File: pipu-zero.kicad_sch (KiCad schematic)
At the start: 4 parts, among them J1 USB_C_Receptacle_USB2.0_14P

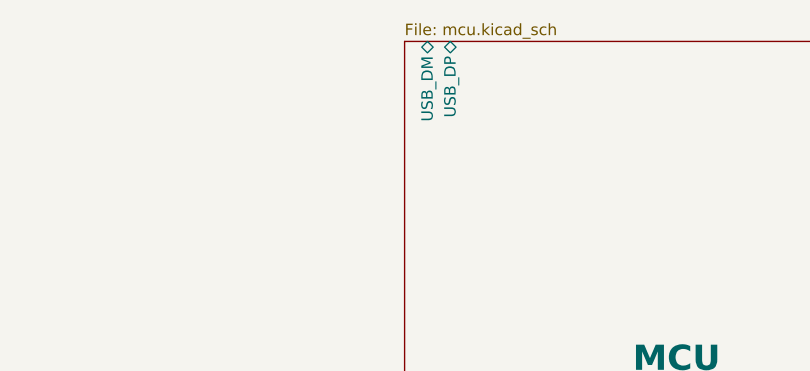
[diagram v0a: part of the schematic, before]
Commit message: add missing connections inside MCU
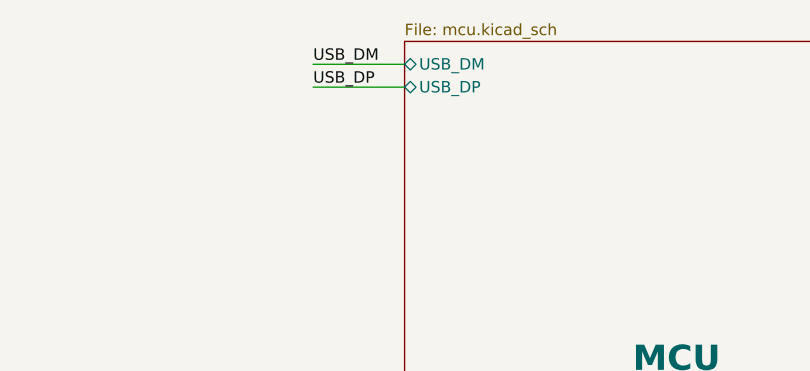
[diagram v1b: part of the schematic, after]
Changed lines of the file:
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@@
+	(wire
+		(pts
+			(xy 138.43 44.45) (xy 148.59 44.45)
+		)
+		(stroke
+			(width 0)
+			(type default)
+		)
+	)
 	(wire
 		(pts
@@
 		(pts
 			(xy 208.28 100.33) (xy 219.71 100.33)
+		)
+		(stroke
+			(width 0)
+			(type default)
+		)
+	)
+	(wire
+		(pts
+			(xy 138.43 46.99) (xy 148.59 46.99)
 		)
 		(stroke
@@
 		)
 	)
+	(label "USB_DM"
+		(at 138.43 44.45 0)
+		(effects
+			(font
+				(size 1.27 1.27)
+			)
+			(justify left bottom)
+		)
+	)
 	(label "USB_VBUS"
 		(at 72.39 85.09 180)
@@
 			)
 			(justify right bottom)
+		)
+	)
+	(label "USB_DP"
+		(at 138.43 46.99 0)
+		(effects
+			(font
+				(size 1.27 1.27)
+			)
+			(justify left bottom)
 		)
 	)
@@
 		)
 		(pin "USB_DM" bidirectional
-			(at 151.13 41.91 90)
-			(effects
-				(font
-					(size 1.27 1.27)
-				)
-				(justify right)
+			(at 148.59 44.45 180)
+			(effects
+				(font
+					(size 1.27 1.27)
+				)
+				(justify left)
 			)
 		)
 		(pin "USB_DP" bidirectional
-			(at 153.67 41.91 90)
-			(effects
-				(font
-					(size 1.27 1.27)
-				)
-				(justify right)
-			)
-		)
+			(at 148.59 46.99 180)
+			(effects
+				(font
+					(size 1.27 1.27)
+				)
+				(justify left)
+			)
+		)

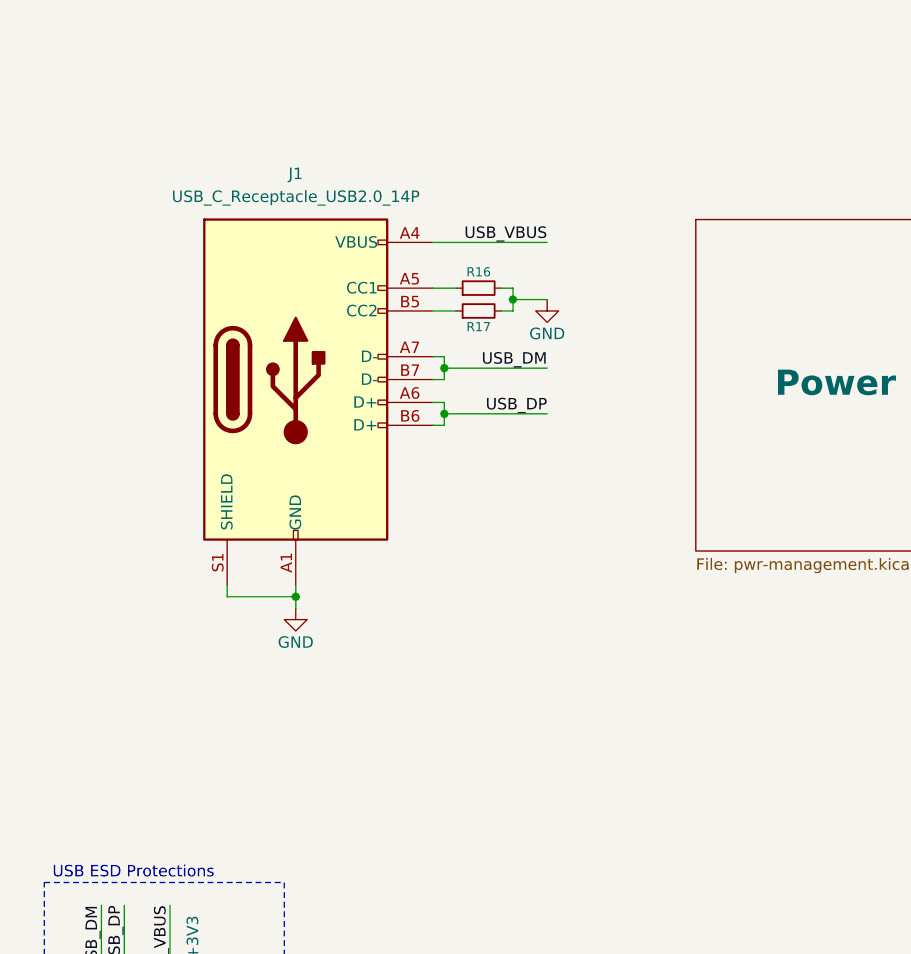
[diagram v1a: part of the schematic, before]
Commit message: add boost converter and ldo regulator
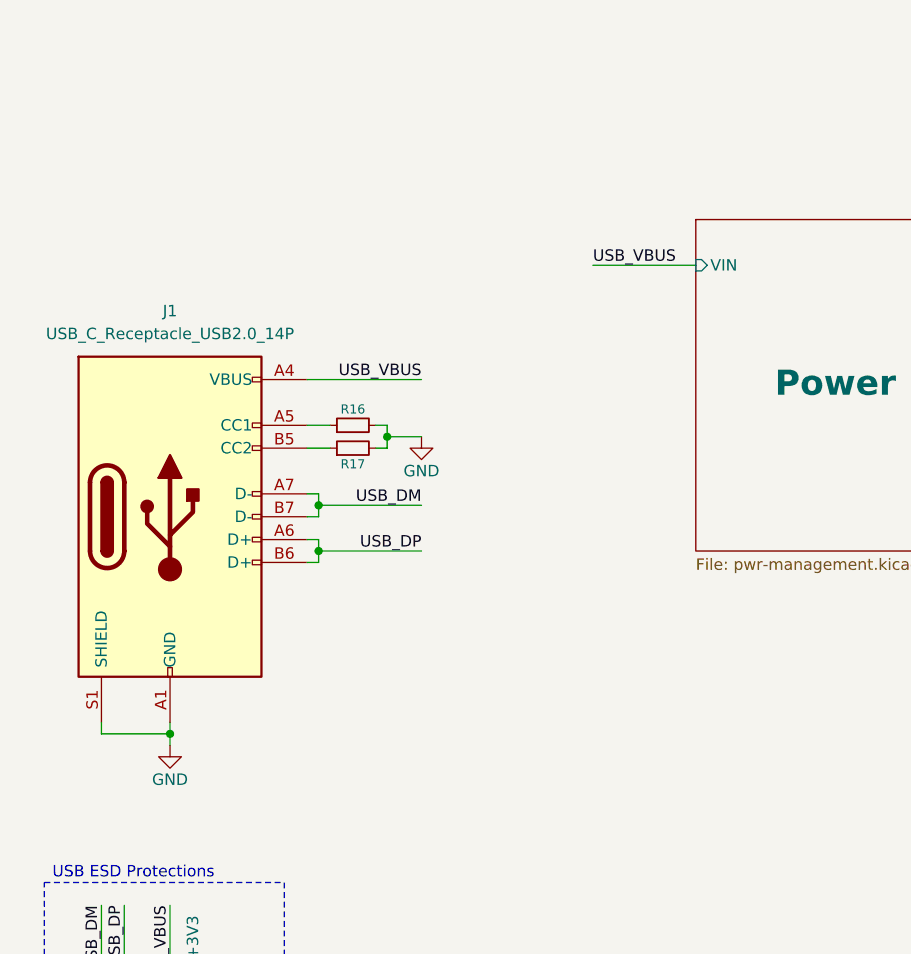
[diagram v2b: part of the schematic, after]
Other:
- sheet Power Manager ports: added VIN; removed none
- moved on the sheet: J1, R16, R17

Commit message: set initial component footprints
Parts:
- R1: renamed from R16; footprint (none) -> Resistor_SMD:R_0603_1608Metric
- R2: renamed from R17; footprint (none) -> Resistor_SMD:R_0603_1608Metric
- renumbered D5 to D1
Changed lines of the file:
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@@
 		(on_board yes)
 		(dnp no)
-		(property "Reference" "R16"
+		(property "Reference" "R1"
 			(at 50.8 103.632 90)
 			(effects
@@
 			)
 		)
-		(property "Footprint" ""
+		(property "Footprint" "Resistor_SMD:R_0603_1608Metric"
 			(at 50.8 105.41 0)
 			(effects
@@
 			(project ""
 				(path "/3130e1f2-bde1-4b12-bd54-0e1e50bd36da"
-					(reference "R16")
+					(reference "R1")
 					(unit 1)
 				)
@@
 		(on_board yes)
 		(dnp no)
-		(property "Reference" "R17"
+		(property "Reference" "R2"
 			(at 50.8 109.728 90)
 			(effects
@@
 			)
 		)
-		(property "Footprint" ""
+		(property "Footprint" "Resistor_SMD:R_0603_1608Metric"
 			(at 50.8 107.95 0)
 			(effects
@@
 			(project "pipu-zero"
 				(path "/3130e1f2-bde1-4b12-bd54-0e1e50bd36da"
-					(reference "R17")
+					(reference "R2")
 					(unit 1)
 				)
@@
 		(on_board yes)
 		(dnp no)
-		(property "Reference" "#PWR035"
+		(property "Reference" "#PWR02"
 			(at 30.48 147.32 0)
 			(effects
@@
 			(project ""
 				(path "/3130e1f2-bde1-4b12-bd54-0e1e50bd36da"
-					(reference "#PWR035")
+					(reference "#PWR02")
 					(unit 1)
 				)
@@
 		(on_board yes)
 		(dnp no)
-		(property "Reference" "#PWR036"
+		(property "Reference" "#PWR04"
 			(at 58.42 113.03 0)
 			(effects
@@
 			(project ""
 				(path "/3130e1f2-bde1-4b12-bd54-0e1e50bd36da"
-					(reference "#PWR036")
+					(reference "#PWR04")
 					(unit 1)
 				)
@@
 		(on_board yes)
 		(dnp no)
-		(property "Reference" "#PWR037"
+		(property "Reference" "#PWR03"
 			(at 33.02 171.45 0)
 			(effects
@@
 			(project ""
 				(path "/3130e1f2-bde1-4b12-bd54-0e1e50bd36da"
-					(reference "#PWR037")
+					(reference "#PWR03")
 					(unit 1)
 				)
@@
 		(on_board yes)
 		(dnp no)
-		(property "Reference" "D5"
+		(property "Reference" "D1"
 			(at 37.338 182.626 90)
 			(effects
@@
 			(project "pipu-zero"
 				(path "/3130e1f2-bde1-4b12-bd54-0e1e50bd36da"
-					(reference "D5")
+					(reference "D1")
 					(unit 1)
 				)
@@
 		(on_board yes)
 		(dnp no)
-		(property "Reference" "#PWR034"
+		(property "Reference" "#PWR01"
 			(at 27.94 193.04 0)
 			(effects
@@
 			(project ""
 				(path "/3130e1f2-bde1-4b12-bd54-0e1e50bd36da"
-					(reference "#PWR034")
-					(unit 1)
-				)
+					(reference "#PWR01")
+					(unit 1)
+				)

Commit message: Add footprints
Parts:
- J1: footprint (none) -> USBC:HRO_TYPE-C-31-M-12
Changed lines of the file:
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@@
 			)
 		)
-		(property "Footprint" ""
+		(property "Footprint" "USBC:HRO_TYPE-C-31-M-12"
 			(at 34.29 115.57 0)
 			(effects

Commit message: modify ios
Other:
- sheet I-O ports: added IO39, IO40, IO41, IO42; removed IO0, IO14, IO3, IO38, IO46, IO9
- sheet MCU ports: added IO39, IO40, IO41, IO42; removed IO0, IO14, IO3, IO38, IO46, IO9
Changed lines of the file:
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@@
-	(wire
-		(pts
-			(xy 208.28 64.77) (xy 219.71 64.77)
-		)
-		(stroke
-			(width 0)
-			(type default)
-		)
-	)
 	(wire
 		(pts
@@
 		(pts
 			(xy 46.99 114.3) (xy 58.42 114.3)
-		)
-		(stroke
-			(width 0)
-			(type default)
-		)
-	)
-	(wire
-		(pts
-			(xy 208.28 62.23) (xy 219.71 62.23)
 		)
 		(stroke
@@
 			)
 		)
-		(pin "IO0" bidirectional
+		(pin "IO39" bidirectional
 			(at 219.71 52.07 180)
 			(effects
@@
 			)
 		)
-		(pin "IO3" bidirectional
+		(pin "IO40" bidirectional
 			(at 219.71 54.61 180)
 			(effects
@@
 			)
 		)
-		(pin "IO9" bidirectional
+		(pin "IO41" bidirectional
 			(at 219.71 57.15 180)
 			(effects
@@
 			)
 		)
-		(pin "IO14" bidirectional
+		(pin "IO42" bidirectional
 			(at 219.71 59.69 180)
-			(effects
-				(font
-					(size 1.27 1.27)
-				)
-				(justify left)
-			)
-		)
-		(pin "IO38" bidirectional
-			(at 219.71 62.23 180)
-			(effects
-				(font
-					(size 1.27 1.27)
-				)
-				(justify left)
-			)
-		)
-		(pin "IO46" bidirectional
-			(at 219.71 64.77 180)
 			(effects
 				(font
@@
 			)
 		)
-		(pin "IO0" bidirectional
-			(at 208.28 52.07 0)
-			(effects
-				(font
-					(size 1.27 1.27)
-				)
-				(justify right)
-			)
-		)
-		(pin "IO3" bidirectional
-			(at 208.28 54.61 0)
-			(effects
-				(font
-					(size 1.27 1.27)
-				)
-				(justify right)
-			)
-		)
-		(pin "IO9" bidirectional
-			(at 208.28 57.15 0)
-			(effects
-				(font
-					(size 1.27 1.27)
-				)
-				(justify right)
-			)
-		)
-		(pin "IO14" bidirectional
-			(at 208.28 59.69 0)
-			(effects
-				(font
-					(size 1.27 1.27)
-				)
-				(justify right)
-			)
-		)
-		(pin "IO38" bidirectional
-			(at 208.28 62.23 0)
-			(effects
-				(font
-					(size 1.27 1.27)
-				)
-				(justify right)
-			)
-		)
-		(pin "IO46" bidirectional
-			(at 208.28 64.77 0)
-			(effects
-				(font
-					(size 1.27 1.27)
-				)
-				(justify right)
-			)
-		)
 		(pin "RXD0" bidirectional
 			(at 208.28 67.31 0)
@@
 			(effects
 				(font
+					(size 1.27 1.27)
+				)
+				(justify right)
+			)
+		)
+		(pin "IO40" bidirectional
+			(at 208.28 54.61 0)
+			(effects
+				(font
+					(size 1.27 1.27)
+				)
+				(justify right)
+			)
+		)
+		(pin "IO41" bidirectional
+			(at 208.28 57.15 0)
+			(effects
+				(font
+					(size 1.27 1.27)
+				)
+				(justify right)
+			)
+		)
+		(pin "IO42" bidirectional
+			(at 208.28 59.69 0)
+			(effects
+				(font
+					(size 1.27 1.27)
+				)
+				(justify right)
+			)
+		)
+		(pin "IO39" bidirectional
+			(at 208.28 52.07 0)
+			(effects
+				(font

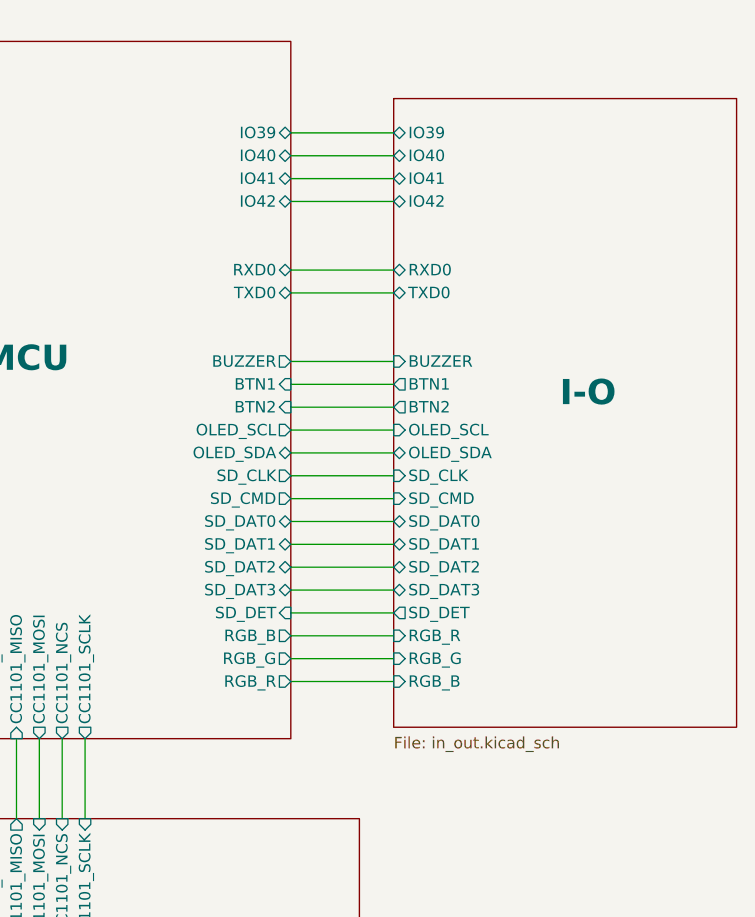
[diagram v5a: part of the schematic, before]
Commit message: Add encoder to schematic
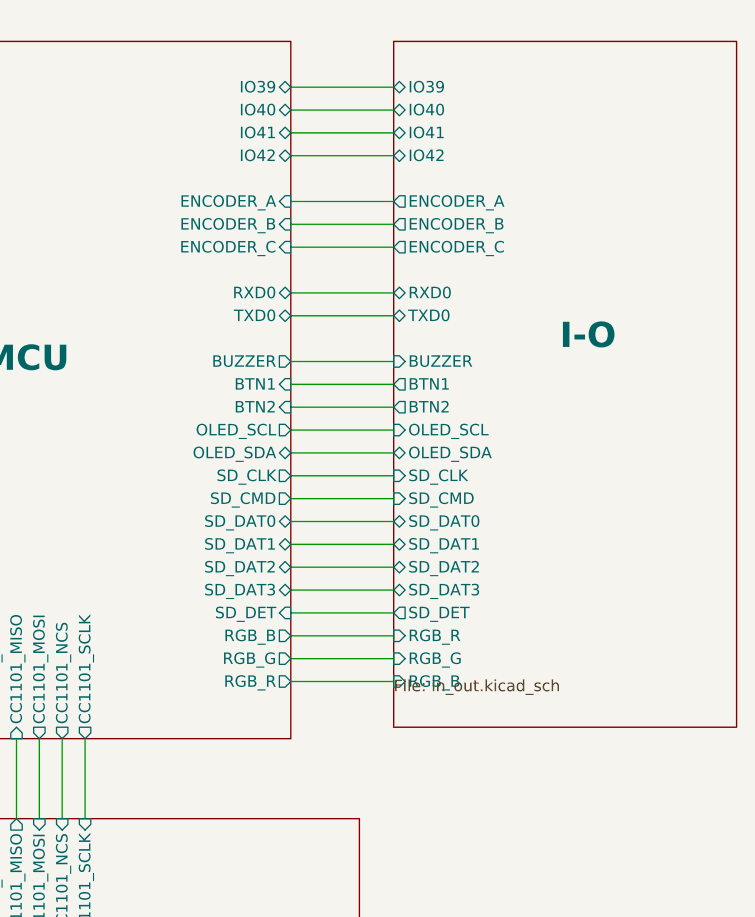
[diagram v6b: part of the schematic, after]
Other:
- sheet I-O ports: added ENCODER_A, ENCODER_B, ENCODER_C; removed none
- sheet MCU ports: added ENCODER_A, ENCODER_B, ENCODER_C; removed none

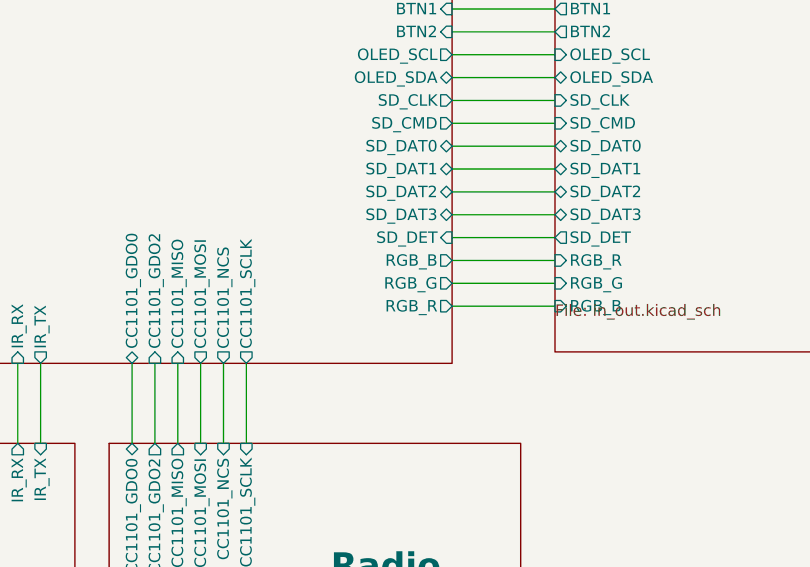
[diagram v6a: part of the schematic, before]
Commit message: component routing
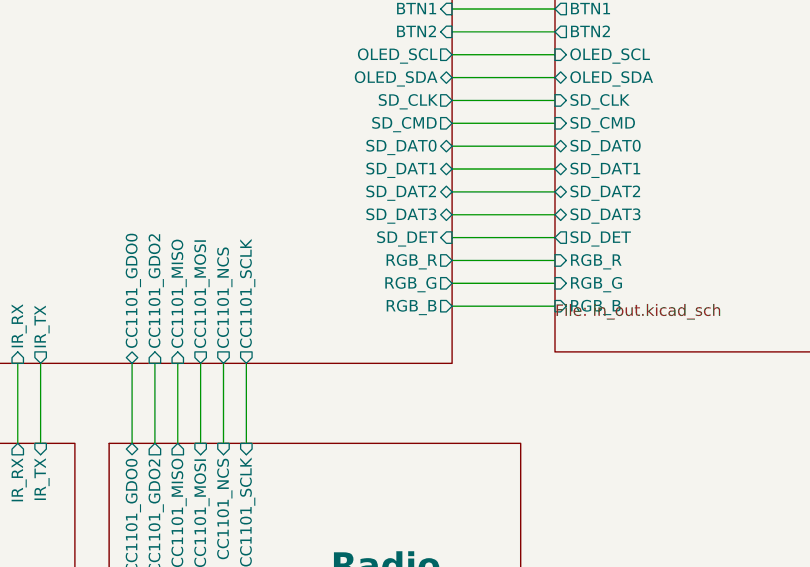
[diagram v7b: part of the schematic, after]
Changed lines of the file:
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@@
 			)
 		)
-		(pin "RGB_B" output
+		(pin "RGB_R" output
 			(at 208.28 107.95 0)
 			(effects
@@
 			)
 		)
-		(pin "RGB_R" output
+		(pin "RGB_B" output
 			(at 208.28 113.03 0)
 			(effects

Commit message: finish routing
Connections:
- net USB_DM renamed USB_D-
- net USB_DP renamed USB_D+
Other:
- sheet MCU ports: added USB_D+, USB_D-; removed USB_DM, USB_DP
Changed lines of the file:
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@@
 		)
 	)
-	(label "USB_DP"
+	(label "USB_D+"
 		(at 25.4 158.75 270)
 		(effects
@@
 		)
 	)
-	(label "USB_DP"
+	(label "USB_D+"
 		(at 58.42 119.38 180)
 		(effects
@@
 		)
 	)
-	(label "USB_DM"
+	(label "USB_D-"
 		(at 138.43 44.45 0)
 		(effects
@@
 		)
 	)
-	(label "USB_DP"
+	(label "USB_D+"
 		(at 138.43 46.99 0)
 		(effects
@@
 		)
 	)
-	(label "USB_DM"
+	(label "USB_D-"
 		(at 58.42 114.3 180)
 		(effects
@@
 		)
 	)
-	(label "USB_DM"
+	(label "USB_D-"
 		(at 22.86 158.75 270)
 		(effects
@@
 			)
 		)
-		(pin "USB_DM" bidirectional
+		(pin "USB_D-" bidirectional
 			(at 148.59 44.45 180)
 			(effects
@@
 			)
 		)
-		(pin "USB_DP" bidirectional
+		(pin "USB_D+" bidirectional
 			(at 148.59 46.99 180)
 			(effects
